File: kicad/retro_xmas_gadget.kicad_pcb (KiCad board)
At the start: 4 copper layers, 76.2 x 101.6 mm, 77 parts, among them J1 USB_C_Receptacle_USB2.0_16P, J2 SD_Card_Receptacle, J3 AudioJack3_SwitchTR, J4 Conn_01x18, J5 Conn_01x02, J6 Conn_01x03, J7 Conn_01x03, J8 Conn_01x07, Q1 UMH3N, Q2 SS8050, SW1 RESET, SW10 SELECT, SW11 START, SW12 A, SW13 B, SW2 BOOT, SW3 KH-SS12F23-G6, SW4 UP, SW5 DOWN, SW6 LEFT, SW7 RIGHT, SW8 MENU, SW9 OPTION, U1 CP2102N-Axx-xQFN28, U2 ESP32-S3-WROOM-1, U4 XC6210B332MR, U5 TP4056

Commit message: baby progress
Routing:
- net /KEY_DOWN: track 69.4 -> 53.6 mm
- net GND: track 89.5 -> 103.0 mm
- net /KEY_LEFT: track 81.2 -> 74.5 mm

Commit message: mayor checks
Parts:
- removed R17: 0, Capacitor_SMD:C_0402_1005Metric
- added R20: 10K, Resistor_SMD:R_0603_1608Metric_Pad0.98x0.95mm_HandSolder, F.Cu at (78.7, 87.2)
- D3, D4: moved to F.Cu
- H1: footprint MountingHole:MountingHole_4.3mm_M4 -> MountingHole:MountingHole_2.7mm_M2.5
- H7: footprint MountingHole:MountingHole_2.5mm -> MountingHole:MountingHole_4.3mm_M4
- moved D3 63.8 mm to (63.5, 124.6)
- moved D4 63.5 mm to (63.5, 121.0)
- moved R22 13.7 mm to (63.5, 130.2)
- moved D2 8.82 mm to (63.5, 128.1)
- moved R19 1.52 mm to (77.2, 87.2)
- moved Q2 1.34 mm to (74.6, 87.2)
- moved R18 1.02 mm to (72.1, 87.2)
- moved R21 0.76 mm to (70.6, 87.2)
- moved J7 0.76 mm to (57.1, 96.5)
- moved R11 0.51 mm to (55.8, 92.7)
- moved R12 0.51 mm to (59.3, 92.7)
- moved R15 0.25 mm to (42.9, 69.3)
- moved R16 0.25 mm to (42.9, 72.9), turned to 90 degrees
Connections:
- J6 pad 1: /VBAT_ON -> /VBAT
- U1 pad 7: Net-(U1-VREGIN) -> VBUS
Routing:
- net Net-(D3-K): track 5.85 -> 88.5 mm, vias 0 -> 3
- net Net-(D4-K): track 12.9 -> 82.3 mm, vias 0 -> 3
- net /VBAT: track 13.5 -> 35.3 mm
- net VBUS: track 59.4 -> 79.9 mm, vias 0 -> 8
- net /KEY_DOWN: track 53.6 -> 69.3 mm
- net /LED_STATUS: track 47.5 -> 60.9 mm
- net /KEY_RIGHT: track 57.6 -> 69.3 mm
- net /VBAT_ON: track 55.9 -> 48.4 mm
- net /KEY_LEFT: track 74.5 -> 81.2 mm
- net /KEY_MENU: track 22.4 -> 28.4 mm
- net /KEY_SELECT: track 16.7 -> 11.0 mm
- net /KEY_UP: track 55.0 -> 60.3 mm
- net /KEY_A: track 32.7 -> 27.6 mm
- net Net-(U1-VDD): track 9.98 -> 6.38 mm
- net /KEY_B: track 39.7 -> 36.4 mm
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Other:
- outline, holes or cut-outs redrawn
- board text added: "A"
- board text added: "B"
- board text added: "BOOT"
- board text added: "GND"
- board text added: "MENU"
- board text added: "OPTION"
- board text added: "RESET"
- board text added: "RX"
- board text added: "SELECT"
- board text added: "START"
- board text added: "TX"
- board text removed: "RESET BOOT LABELS"
- board text removed: "SPEAKER CUTOUTS"

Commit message: almost complete
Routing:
- net GND: vias 175 -> 190
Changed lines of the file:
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@@
 		)
 		(embedded_fonts no)
-		(model "${KICAD9_3DMODEL_DIR}/Package_SO.3dshapes/SOP-8-1EP_4.57x4.57mm_P1.27mm_EP4.57x4.45mm.step"
+		(model "${KICAD9_3DMODEL_DIR}/Package_SO.3dshapes/SOIC-8_5.3x6.2mm_P1.27mm.step"
 			(offset
 				(xyz 0 0 0)
@@
 		)
 		(embedded_fonts no)
-		(model "${KICAD9_3DMODEL_DIR}/Package_SO.3dshapes/SOP-8-1EP_4.57x4.57mm_P1.27mm_EP4.57x4.45mm.step"
+		(model "${KICAD9_3DMODEL_DIR}/Package_SO.3dshapes/SOIC-8_5.3x5.3mm_P1.27mm.step"
 			(offset
 				(xyz 0 0 0)
@@
 	)
 	(via
+		(at 71.501 124.46)
+		(size 0.6)
+		(drill 0.3)
+		(layers "F.Cu" "B.Cu")
+		(free yes)
+		(net 4)
+	)
+	(via
 		(at 93.98 119.38)
 		(size 0.8)
@@
 	)
 	(via
+		(at 81.407 129.794)
+		(size 0.6)
+		(drill 0.3)
+		(layers "F.Cu" "B.Cu")
+		(free yes)
+		(net 4)
+	)
+	(via
 		(at 32.766 99.568)
 		(size 0.6)
@@
 	)
 	(via
+		(at 94.488 109.474)
+		(size 0.6)
+		(drill 0.3)
+		(layers "F.Cu" "B.Cu")
+		(free yes)
+		(net 4)
+	)
+	(via
 		(at 43.434 132.08)
 		(size 0.6)
@@
 	)
 	(via
+		(at 72.009 129.794)
+		(size 0.6)
+		(drill 0.3)
+		(layers "F.Cu" "B.Cu")
+		(free yes)
+		(net 4)
+	)
+	(via
 		(at 88.392 98.679)
 		(size 0.6)
@@
 	)
 	(via
+		(at 55.626 127.635)
+		(size 0.6)
+		(drill 0.3)
+		(layers "F.Cu" "B.Cu")
+		(free yes)
+		(net 4)
+	)
+	(via
 		(at 99.06 139.7)
 		(size 0.8)
@@
 	)
 	(via
+		(at 46.609 113.792)
+		(size 0.6)
+		(drill 0.3)
+		(layers "F.Cu" "B.Cu")
+		(free yes)
+		(net 4)
+	)
+	(via
 		(at 99.06 129.54)
 		(size 0.8)
@@
 	)
 	(via
+		(at 85.852 109.728)
+		(size 0.6)
+		(drill 0.3)
+		(layers "F.Cu" "B.Cu")
+		(free yes)
+		(net 4)
+	)
+	(via
 		(at 27.94 93.98)
 		(size 0.8)
@@
 	)
 	(via
+		(at 83.947 118.745)
+		(size 0.6)
+		(drill 0.3)
+		(layers "F.Cu" "B.Cu")
+		(free yes)
+		(net 4)
+	)
+	(via
 		(at 74.295 85.852)
 		(size 0.8)
@@
 	)
 	(via
+		(at 85.852 117.856)
+		(size 0.6)
+		(drill 0.3)
+		(layers "F.Cu" "B.Cu")
+		(free yes)
+		(net 4)
+	)
+	(via
 		(at 94.996 104.013)
 		(size 0.6)
@@
 	)
 	(via
+		(at 78.867 113.538)
+		(size 0.6)
+		(drill 0.3)
+		(layers "F.Cu" "B.Cu")
+		(free yes)
+		(net 4)
+	)
+	(via
 		(at 36.068 124.587)
 		(size 0.6)
@@
 	)
 	(via
+		(at 94.996 125.603)
+		(size 0.6)
+		(drill 0.3)
+		(layers "F.Cu" "B.Cu")
+		(free yes)
+		(net 4)
+	)
+	(via
 		(at 71.755 112.395)
 		(size 0.6)
@@
 	)
 	(via
+		(at 82.677 109.728)
+		(size 0.6)
+		(drill 0.3)
+		(layers "F.Cu" "B.Cu")
+		(free yes)
+		(net 4)
+	)
+	(via
 		(at 83.82 70.866)
 		(size 0.8)
@@
 	)
 	(via
+		(at 85.598 125.603)
+		(size 0.6)
+		(drill 0.3)
+		(layers "F.Cu" "B.Cu")
+		(free yes)
+		(net 4)
+	)
+	(via
 		(at 68.58 53.34)
 		(size 0.8)
@@
 	)
 	(via
+		(at 46.228 127.762)
+		(size 0.6)
+		(drill 0.3)
+		(layers "F.Cu" "B.Cu")
+		(free yes)
+		(net 4)
+	)
+	(via
 		(at 27.94 53.34)
 		(size 0.8)
@@
 		(size 0.6)
 		(drill 0.3)
+		(layers "F.Cu" "B.Cu")
+		(free yes)
+		(net 4)
+	)
+	(via
+		(at 39.37 127.889)
+		(size 0.6)
+		(drill 0.3)

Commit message: run down checking points
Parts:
- added C17: 100nf, Capacitor_SMD:C_0603_1608Metric_Pad1.08x0.95mm_HandSolder, B.Cu at (31.0, 76.5)
- added R17: 15k, Resistor_SMD:R_0603_1608Metric_Pad0.98x0.95mm_HandSolder, B.Cu at (29.1, 76.5)
- added R23: 5.1k, Resistor_SMD:R_0603_1608Metric_Pad0.98x0.95mm_HandSolder, B.Cu at (32.9, 76.5)
- moved J6 1.07 mm to (38.9, 78.2)
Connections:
- U3 pad 9: unconnected-(U3-EP-Pad9)_1 -> GND
- U5 pad 1: GND -> Net-(U5-TEMP)
- U5 pad 9: unconnected-(U5-EP-Pad9)_5 -> GND
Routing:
- net Net-(U5-TEMP): track 0.00 -> 6.73 mm
- net GND: track 103.2 -> 105.1 mm, vias 190 -> 197
- net VBUS: track 79.9 -> 81.7 mm, vias 8 -> 9
- net Net-(D4-K): track 82.3 -> 83.7 mm
- net /VBAT: track 35.3 -> 34.1 mm
- net Net-(D3-K): track 88.5 -> 89.3 mm
- net VCC: track 23.9 -> 24.7 mm

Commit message: final improvements and checks
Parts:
- H7: footprint MountingHole:MountingHole_4.3mm_M4 -> MountingHole:MountingHole_3.5mm
- J5: footprint Connector_JST:JST_SH_SM02B-SRSS-TB_1x02-1MP_P1.00mm_Horizontal -> AMPHENOL_10114830-10102LF:AMPHENOL_10114830-10102LF
- J6: footprint Connector_JST:JST_GH_SM03B-GHS-TB_1x03-1MP_P1.25mm_Horizontal -> AMPHENOL_10114830-10103LF:AMPHENOL_10114830-10103LF
- L1: footprint Inductor_SMD:L_0603_1608Metric_Pad1.05x0.95mm_HandSolder -> Inductor_SMD:L_0805_2012Metric_Pad1.05x1.20mm_HandSolder
- moved L1 4.08 mm to (77.7, 66.7)
- moved C16 3.18 mm to (82.4, 66.7), turned to 180 degrees
- moved J5 1.38 mm to (79.4, 71.8)
- moved H6 1.27 mm to (52.1, 57.1)
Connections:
- net DTR renamed /DTR
- net RTS renamed /RTS
- C17 pad 2: Net-(U5-TEMP) -> /Temp
- J5 pad 1: /SPK+ -> /AUDIO-
- J5 pad 2: /AUDIO- -> /SPK+
- J6 pad 2: unconnected-(J6-Pin_2-Pad2) -> /Temp
- R17 pad 1: Net-(U5-TEMP) -> /Temp
- R23 pad 2: Net-(U5-TEMP) -> /Temp
- U5 pad 1: Net-(U5-TEMP) -> /Temp
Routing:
- net /Temp: track 0.00 -> 14.6 mm
- net Net-(U5-TEMP): track 6.73 -> 0.00 mm
- net VCC: track 24.7 -> 29.2 mm
- net /TFT_CS: track 26.6 -> 23.4 mm
- net /TFT_DC: track 24.5 -> 22.4 mm
- net /TFT_SDI: track 24.3 -> 22.5 mm
- net /TFT_SCL: track 24.2 -> 22.6 mm
- net /KEY_LEFT: track 81.2 -> 79.6 mm
- net /TFT_RST: track 34.4 -> 32.8 mm
- net /BOOT: track 21.0 -> 22.3 mm
- net VAA: track 8.68 -> 9.72 mm, vias 3 -> 4
- net Net-(U1-D-): track 12.9 -> 13.8 mm
- net /AUDIO-: track 28.3 -> 29.2 mm
- net /TFT_LED: track 16.0 -> 15.1 mm
- net /IO1: track 75.1 -> 75.9 mm
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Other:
- board text added: "+T-"
- board text added: "IO1"
- board text added: "IO19"
- board text added: "IO2"
- board text added: "IO20"
- board text added: "IO21"
- board text added: "VCC"

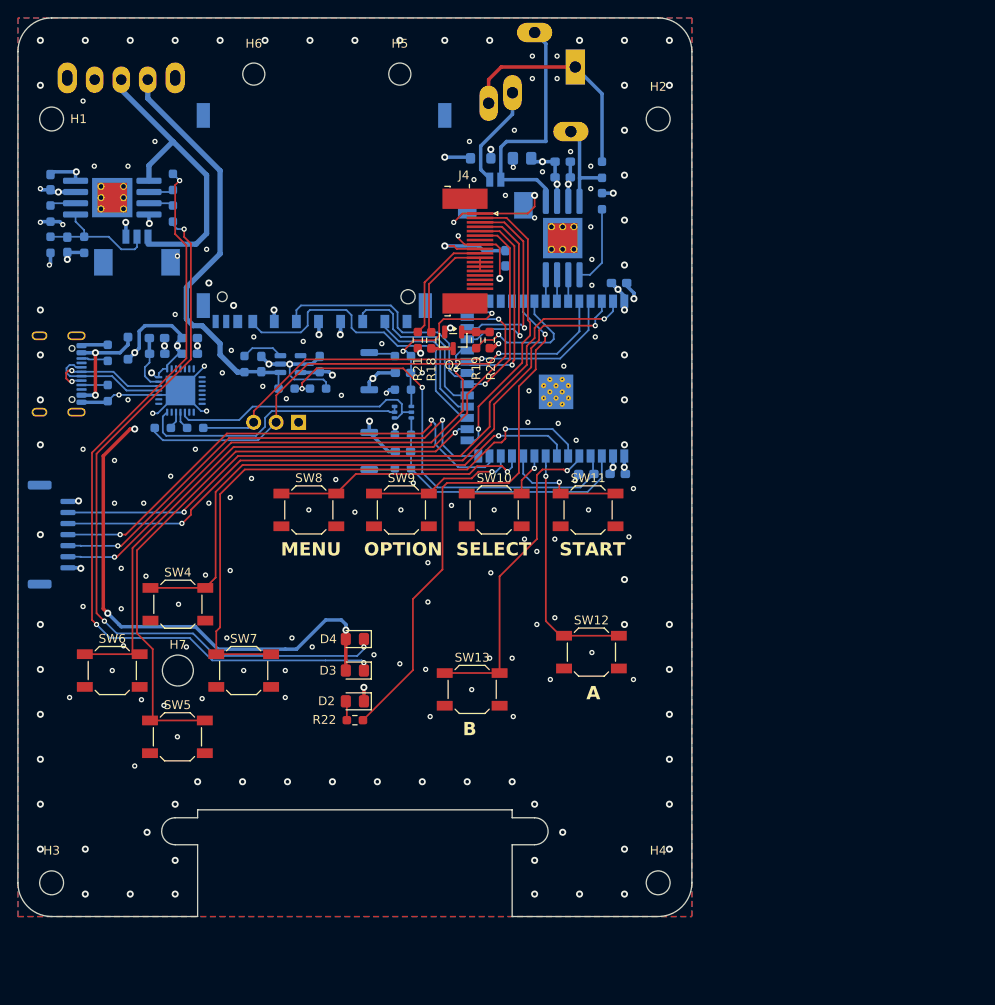
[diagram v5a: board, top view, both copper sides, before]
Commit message: speaker placement
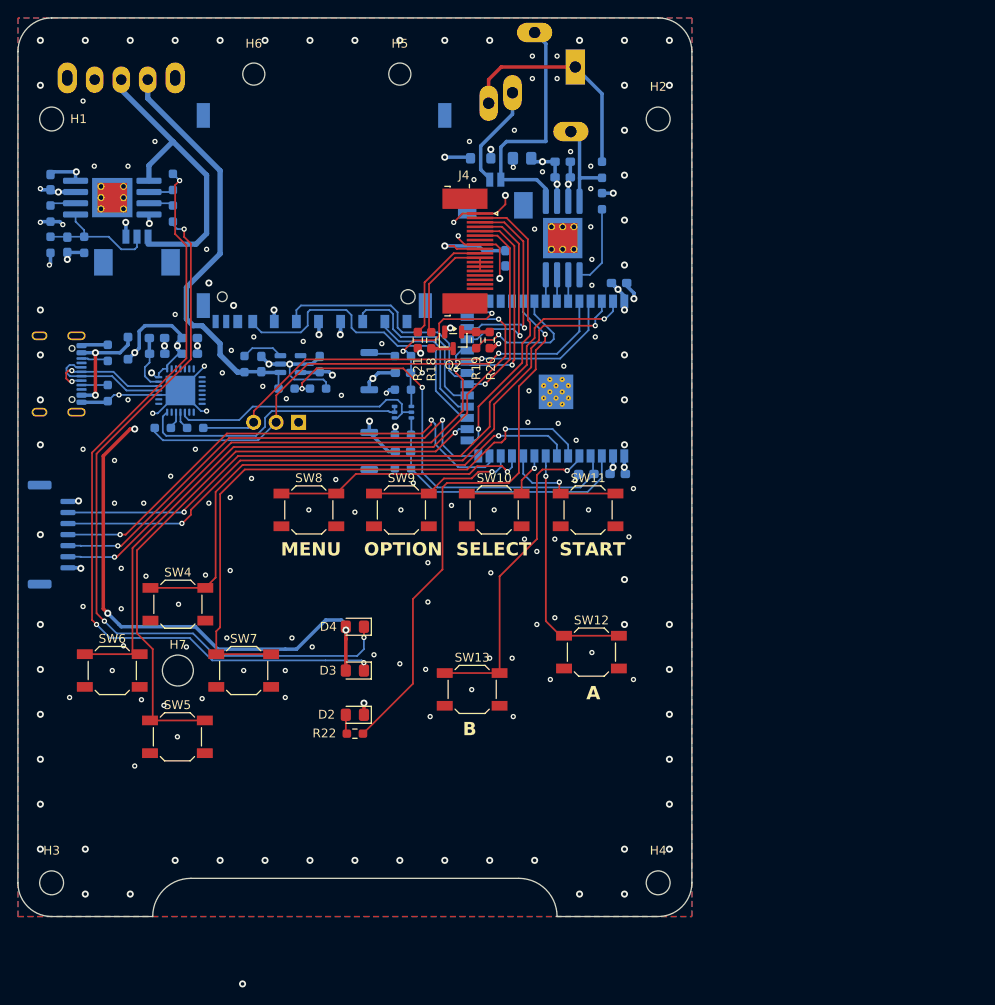
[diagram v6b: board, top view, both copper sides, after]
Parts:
- moved D2 1.52 mm to (63.5, 129.6)
- moved R22 1.52 mm to (63.5, 131.7)
- moved D4 1.40 mm to (63.5, 119.6)
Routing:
- net GND: track 105.1 -> 100.0 mm, vias 197 -> 188
- net /LED_STATUS: track 61.0 -> 62.5 mm
- net Net-(D4-K): track 83.7 -> 85.1 mm
- net (no net): vias 0 -> 1
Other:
- outline, holes or cut-outs redrawn

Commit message: final design, with decals
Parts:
- added G***: LOGO, LOGO, F.Cu at (43.3, 106.8)
- added G***: LOGO, LOGO, F.Cu at (87.0, 134.6)
- added G***: LOGO, LOGO, B.Cu at (35.7, 63.8)
- added G***: LOGO, LOGO, B.Cu at (95.0, 56.4)
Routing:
- net GND: vias 188 -> 190
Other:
- board text added: "RETRO GAMING GADGET"
- board text added: "https://github.com/ducalex/retro-go PCB v0.9 by hfvermeer"
